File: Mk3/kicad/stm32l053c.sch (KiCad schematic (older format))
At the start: 29 parts, among them J1 LIGHT+, J2 LIGHT-, P1 SWD, U1 AP2112, U2 STM32L053C8_LQFP48, U3 ADS1015, U4 UFL_SMA, U5 RFM92/95

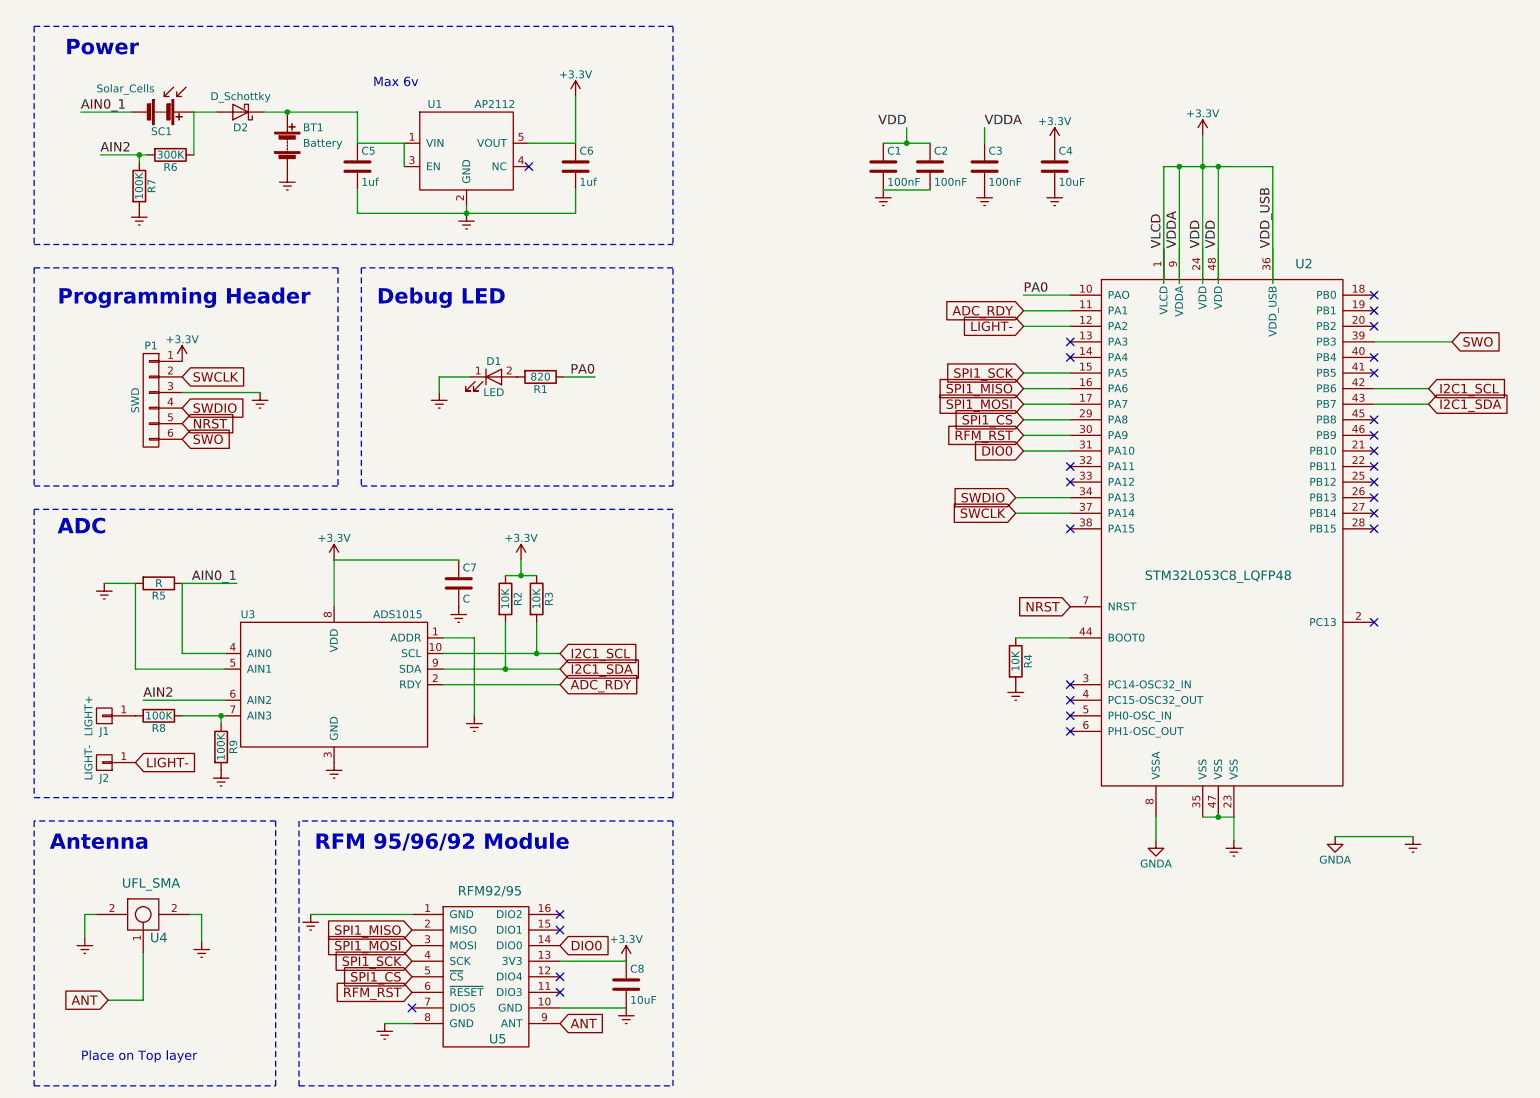
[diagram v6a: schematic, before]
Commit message: Bigger board
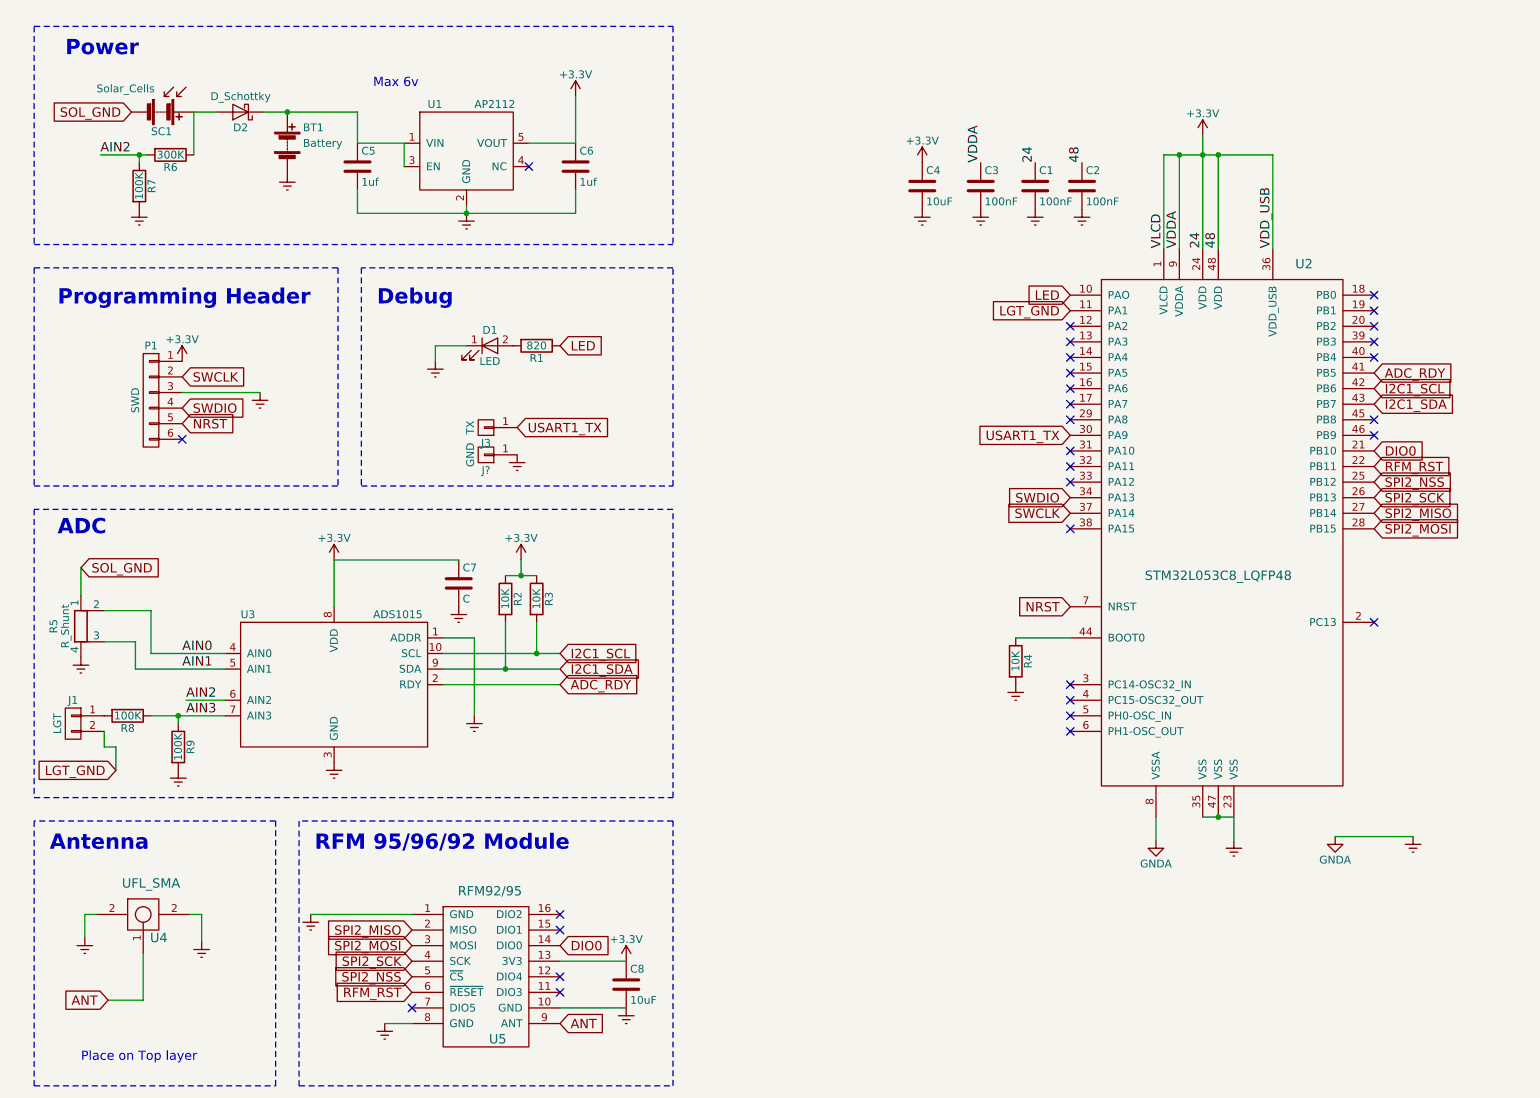
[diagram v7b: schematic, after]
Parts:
- removed J1: LIGHT+, Pin_Headers:Pin_Header_Straight_1x01_Pitch2.54mm, symbol CONN_01X01
- removed J2: LIGHT-, Pin_Headers:Pin_Header_Straight_1x01_Pitch2.54mm, symbol CONN_01X01
- removed R5: R, Resistors_SMD:R_1206_HandSoldering, symbol R
- added J1: LGT, Pin_Headers:Pin_Header_Straight_1x02_Pitch2.54mm, symbol CONN_01X02
- added J3: TX, Pin_Headers:Pin_Header_Straight_1x01_Pitch2.54mm, symbol CONN_01X01
- added J?: GND, Pin_Headers:Pin_Header_Straight_1x01_Pitch2.54mm, symbol CONN_01X01
- added R5: R_Shunt, theapi:SHUNT_1210_HandSoldering, symbol R_Shunt
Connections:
- net labels added: 24, 48, AIN0, AIN1, AIN3, LED, LGT_GND, SOL_GND, SPI2_MISO, SPI2_MOSI, SPI2_NSS, SPI2_SCK, USART1_TX
- net labels removed: AIN0_1, LIGHT-, PA0, SPI1_CS, SPI1_MISO, SPI1_MOSI, SPI1_SCK, SWO, VDD
- wire segments 78 -> 62
- no-connect marks 29 -> 30
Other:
- note added: "Debug"
- note removed: "Debug LED"
- moved on the sheet: C1, C2, C3, C4, D1, R1, R8, R9

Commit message: Routing
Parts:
- D2: footprint Diodes_SMD:D_0805 -> Diodes_SMD:D_1206
- gave numbers to parts that had none: 1
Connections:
- net DIO0: now also U2.33 (PA12); no longer U2.21 (PB10)
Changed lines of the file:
@@
 NoConn ~ 7625 2850
 NoConn ~ 7625 3550
-NoConn ~ 7625 3650
 NoConn ~ 7625 3950
 NoConn ~ 9575 2550
@@
 F 0 "D2" H 2300 1375 50  0000 C CNN
 F 1 "D_Schottky" H 2300 1175 50  0000 C CNN
-F 2 "Diodes_SMD:D_0805" H 2300 1275 50  0001 C CNN
+F 2 "Diodes_SMD:D_1206" H 2300 1275 50  0001 C CNN
 F 3 "" H 2300 1275 50  0001 C CNN
 	1    2300 1275
@@
 Text GLabel 4350 6625 2    60   Input ~ 0
 DIO0
-Text GLabel 9575 3450 2    60   Input ~ 0
+Text GLabel 7625 3650 0    60   Input ~ 0
 DIO0
 $Comp
@@
 	1275 4200 1275 4375
 $Comp
-L CONN_01X01 J?
+L CONN_01X01 J2
 U 1 1 593799A7
 P 3875 3475
-F 0 "J?" H 3875 3575 50  0000 C CNN
+F 0 "J2" H 3875 3575 50  0000 C CNN
 F 1 "GND" V 3975 3475 50  0000 C CNN
 F 2 "Pin_Headers:Pin_Header_Straight_1x01_Pitch2.54mm" H 3875 3475 50  0001 C CNN
@@
 $EndComp
 $Comp
-L Earth #PWR?
+L Earth #PWR032
 U 1 1 59379ABF
 P 4075 3475
-F 0 "#PWR?" H 4075 3225 50  0001 C CNN
+F 0 "#PWR032" H 4075 3225 50  0001 C CNN
 F 1 "Earth" H 4075 3325 50  0001 C CNN
 F 2 "" H 4075 3475 50  0000 C CNN
@@
 	-1   0    0    -1
 $EndComp
+NoConn ~ 9575 3450
 $EndSCHEMATC
